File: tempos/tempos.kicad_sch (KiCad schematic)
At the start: 16 parts, among them SW1 SW_Push, SW2 SW_Push, SW3 SW_DIP_x01, U1 WeMos_D1_mini, U2 74HC595, U5 CD4051B

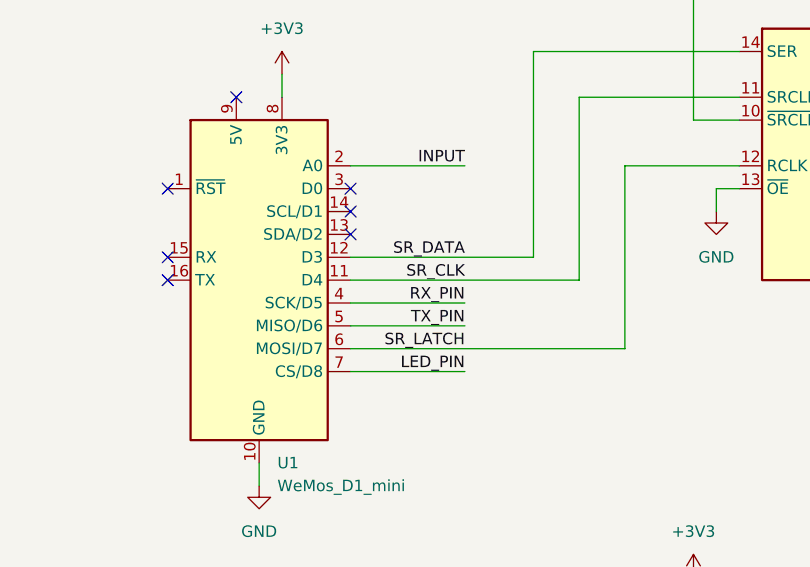
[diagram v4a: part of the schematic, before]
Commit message: tempos: New LED pin assignment
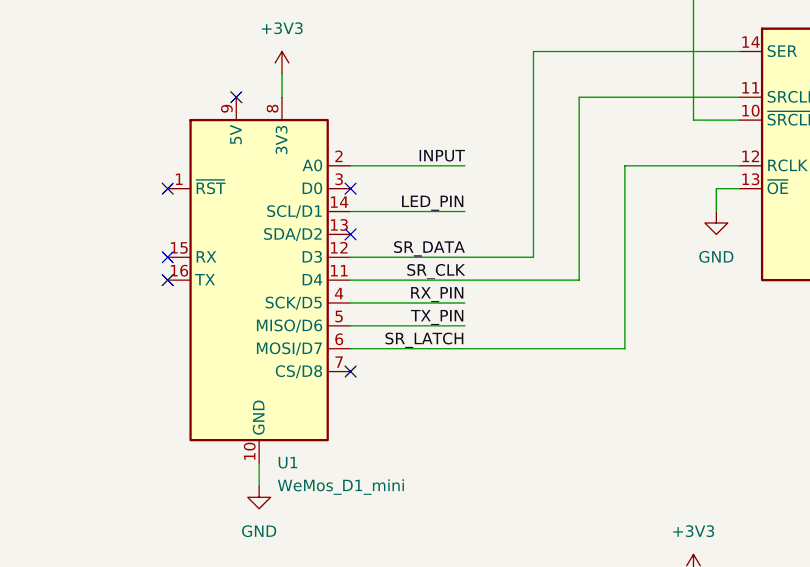
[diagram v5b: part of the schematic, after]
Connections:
- net LED_PIN: now also U1.14 (SCL/D1); no longer U1.7 (CS/D8)
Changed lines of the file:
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@@
   (title_block
     (title "tempos single node")
-    (date "2022-12-22")
-    (rev "v1.2")
+    (date "2022-12-23")
+    (rev "v1.3")
     (company "Malmö Universitet, Fakulteten för teknik och samhälle")
     (comment 3 "Copyright: Malmö Universitet")
@@
   (no_connect (at 71.12 58.42))
   (no_connect (at 50.8 66.04))
-  (no_connect (at 71.12 60.96))
   (no_connect (at 71.12 63.5))
+  (no_connect (at 71.12 78.74))
   (no_connect (at 134.62 60.96))
   (no_connect (at 50.8 68.58))
@@
     (stroke (width 0) (type default) (color 0 0 0 0))
   )
-  (wire (pts (xy 71.12 78.74) (xy 83.82 78.74))
+  (wire (pts (xy 71.12 60.96) (xy 83.82 60.96))
     (stroke (width 0) (type default) (color 0 0 0 0))
   )
@@
     (effects (font (size 1.27 1.27)) (justify right bottom))
   )
-  (label "LED_PIN" (at 83.82 78.74 180)
-    (effects (font (size 1.27 1.27)) (justify right bottom))
-  )
+  (label "LED_PIN" (at 83.82 60.96 180)
+    (effects (font (size 1.27 1.27)) (justify right bottom))
+  )
